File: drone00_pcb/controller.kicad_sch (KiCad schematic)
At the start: 6 parts, among them SW1 SW_Push, U2 STM8S003F3P

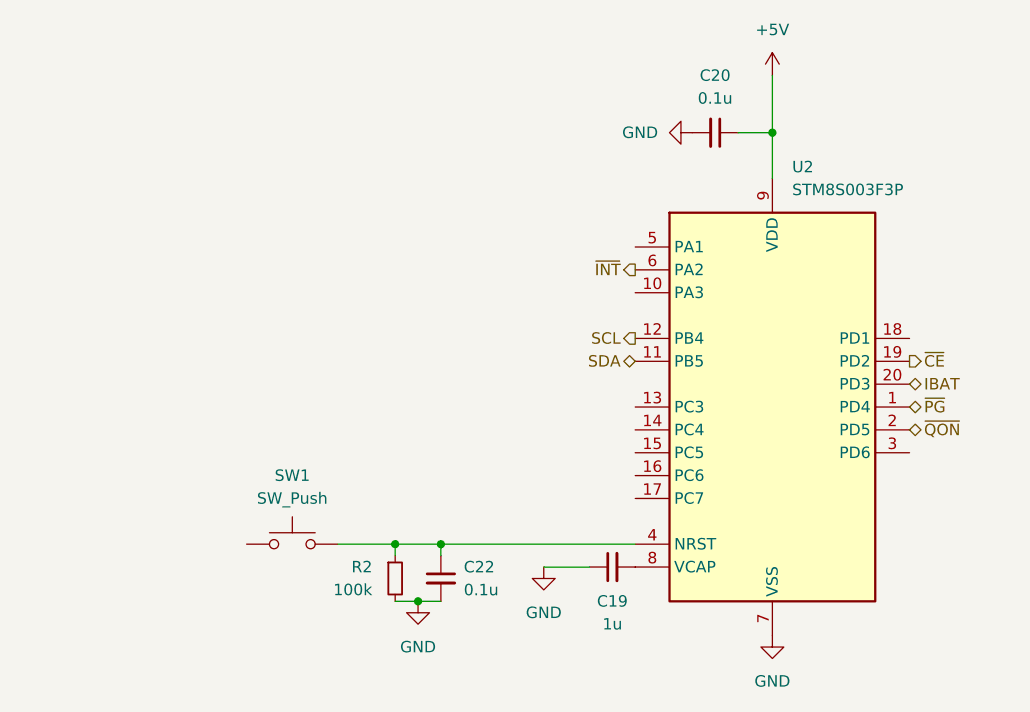
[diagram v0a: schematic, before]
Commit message: Add BQ24
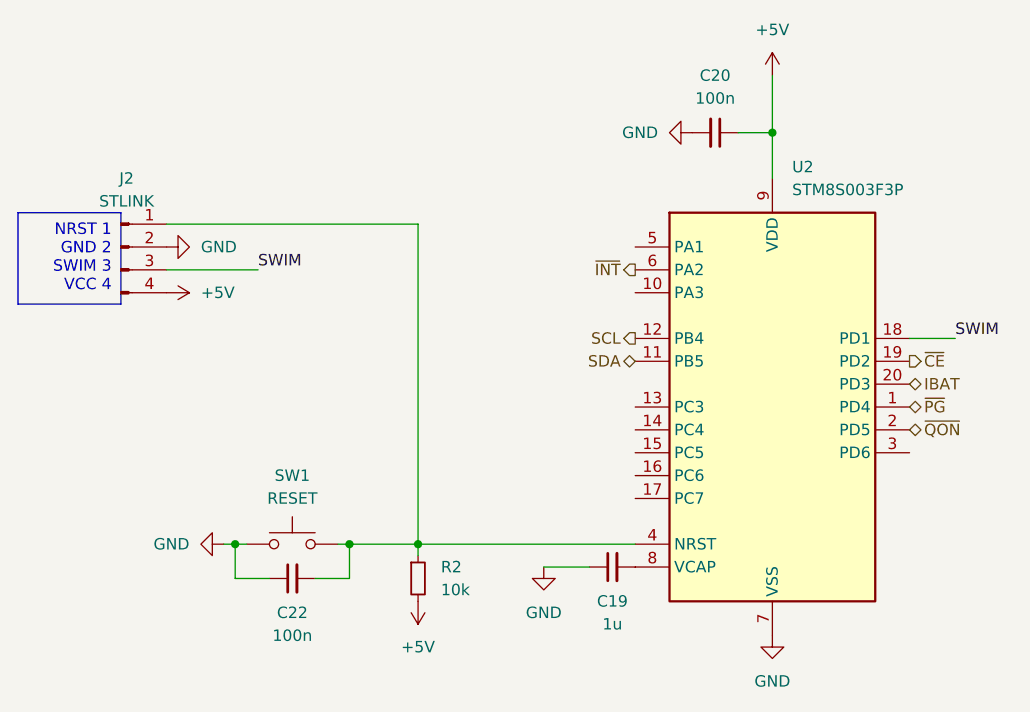
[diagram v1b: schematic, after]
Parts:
- added J2: STLINK, Connector_PinHeader_2.54mm:PinHeader_1x04_P2.54mm_Vertical, symbol Connector:Conn_01x04_Pin
- C19: footprint (none) -> Capacitor_SMD:C_0402_1005Metric; LCSC Part # (none) -> C52923
- C20, C22: value 0.1u -> 100n; footprint (none) -> Capacitor_SMD:C_0402_1005Metric; LCSC Part # (none) -> C1525
- R2: value 100k -> 10k; footprint (none) -> Resistor_SMD:R_0402_1005Metric; LCSC Part # (none) -> C25744
- SW1: value SW_Push -> RESET
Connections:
- net +5V: now also R2.2, J2.4 (Pin_4)
- net GND: now also C22.1, SW1.1, J2.2 (Pin_2); no longer C22.2, R2.2
- net at R2.1, SW1.2, U2.4 (NRST): now also C22.2, J2.1 (Pin_1); no longer C22.1
- net SWIM: now reaches U2.18 (PD1)
- net SWIM: now also J2.3 (Pin_3)
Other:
- moved on the sheet: R2

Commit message: Finish footprints
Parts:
- SW1: footprint (none) -> Button_Switch_SMD:SW_Push_1P1T_XKB_TS-1187A; LCSC Part # (none) -> C318884
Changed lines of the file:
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@@
       (effects (font (size 1.27 1.27)))
     )
-    (property "Footprint" "" (at 80.01 93.98 0)
+    (property "Footprint" "Button_Switch_SMD:SW_Push_1P1T_XKB_TS-1187A" (at 80.01 93.98 0)
       (effects (font (size 1.27 1.27)) hide)
     )
@@
       (effects (font (size 1.27 1.27)) hide)
     )
-    (property "LCSC Part #" "" (at 80.01 99.06 0)
+    (property "LCSC Part #" "C318884" (at 80.01 99.06 0)
       (effects (font (size 1.27 1.27)) hide)
     )
